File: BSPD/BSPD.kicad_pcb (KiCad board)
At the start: 2 copper layers, 81 x 61 mm, 34 parts, among them Q101 Q_PMOS_GSD, U101 641964-1, U102 641964-1, U103 R-78E5.0-0.5, U104 SN74LVC1G08DBVR, U105 LM339DR, U106 NE555DR, U107 SN74LVC3G14DCUR, U108 SN74AC32DR, U109 SN74LVC1G08DBVR, U110 641964-1, U111 641964-1

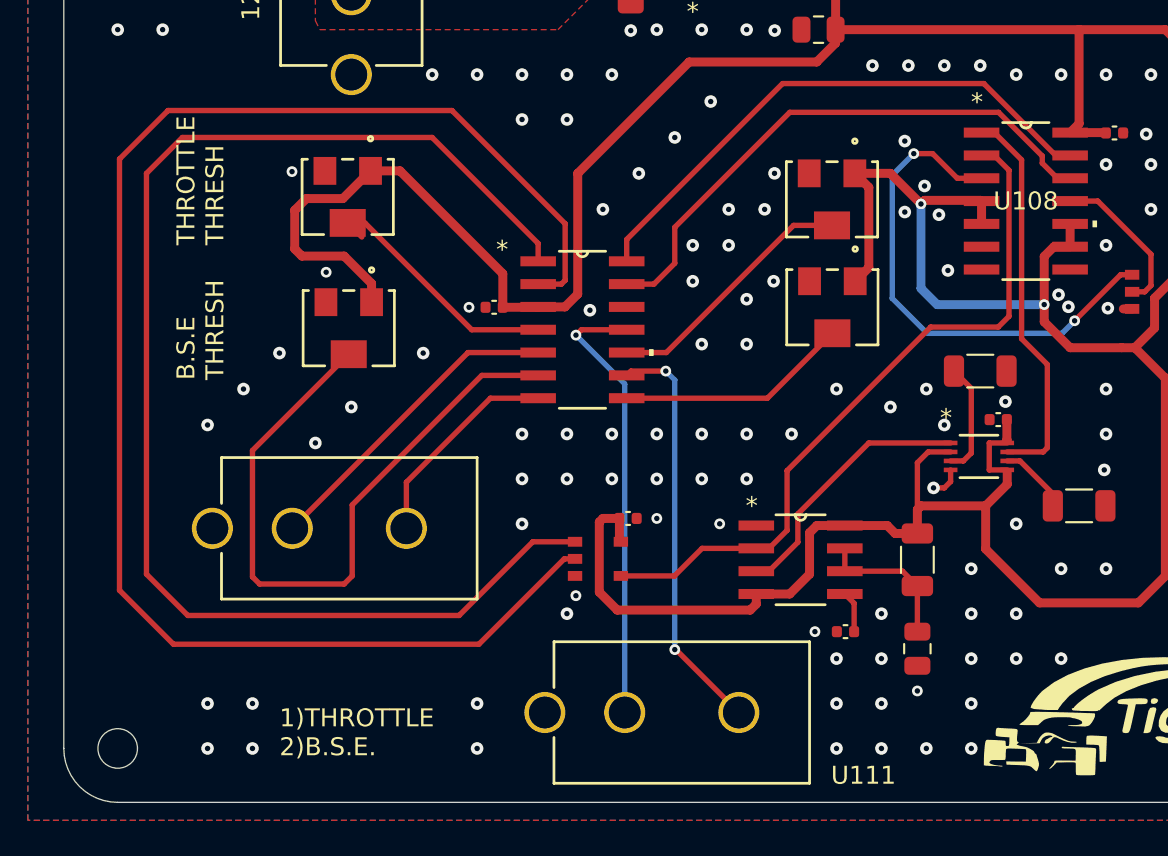
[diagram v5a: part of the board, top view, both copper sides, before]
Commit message: Fault Latch Updated and generated gerber files
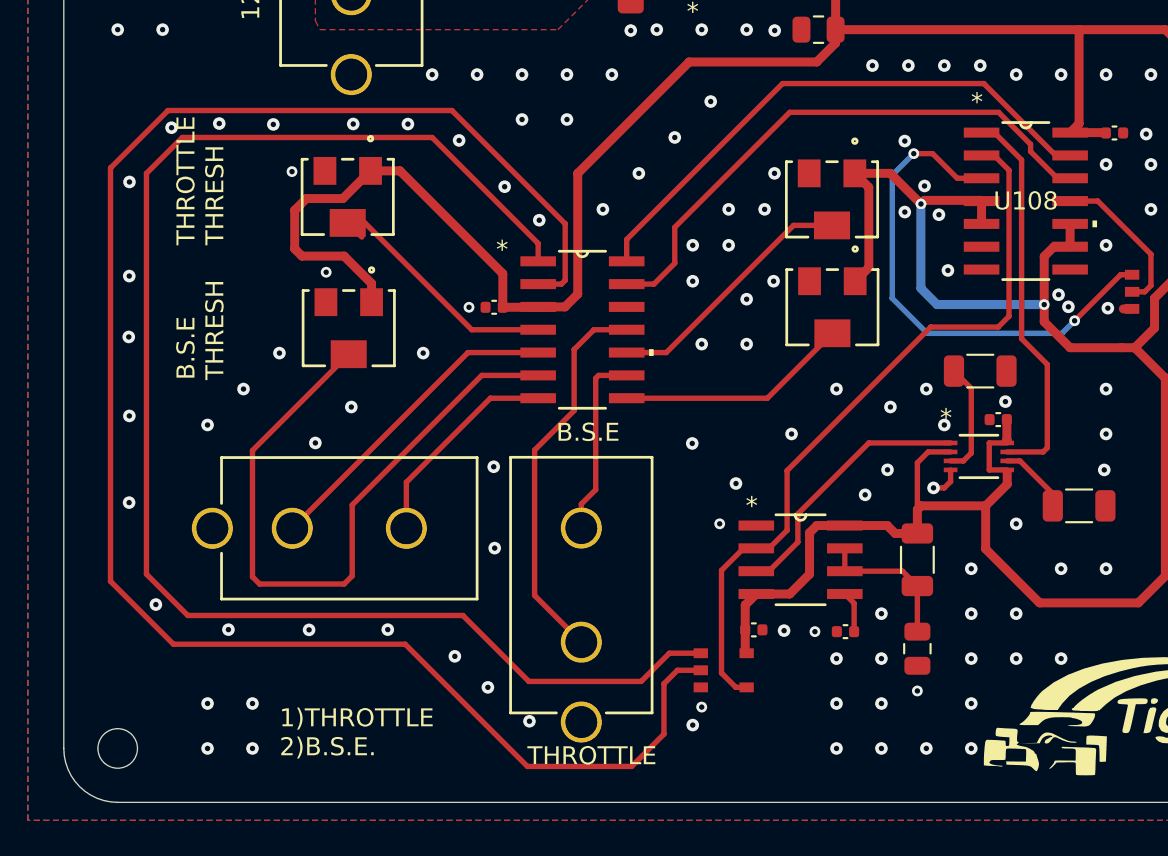
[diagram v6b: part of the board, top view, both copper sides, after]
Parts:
- U108: footprint LM339DR:D14 -> SN74AC32DR:D14
- moved C103 9.35 mm to (159.1, 126.5)
- moved U104 9.35 mm to (157.4, 128.8)
- moved U111 4.60 mm to (149.5, 127.2), turned to 90 degrees
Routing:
- net +5V: track 230.1 -> 217.4 mm
- net 2OUT: track 85.9 -> 98.0 mm
- net BSE_Sense_IN: track 23.0 -> 11.0 mm, vias 2 -> 0
- net 1OUT: track 74.9 -> 82.3 mm
- net THROTTLE_Sense_IN: track 25.1 -> 21.7 mm, vias 1 -> 0
- net Net-(U104-Y): track 39.5 -> 41.2 mm
- net GND: vias 268 -> 278
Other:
- board text added: "B.S.E"
- board text added: "THROTTLE"

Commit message: Labeling for clarithy
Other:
- board text added: "1)THRTL MIN VOLTAGE 2)B.S.E. MIN VOLTAGE"
- board text added: "1)THRTL SENSE 2)B.S.E. SENSE"
- board text added: "10% THROTTLE"
- board text added: "HARD BREAK"
- board text removed: "1)THROTTLE 2)B.S.E."
- board text removed: "B.S.E"
- board text removed: "THROTTLE"
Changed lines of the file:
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@@
 		(layer "Edge.Cuts")
 	)
-	(gr_text "1)THROTTLE\n2)B.S.E."
-		(at 132.7 133.6 0)
+	(gr_text "1)THRTL SENSE\n2)B.S.E. SENSE\n"
+		(at 151.2 134.6 0)
 		(layer "F.SilkS" knockout)
 		(effects
@@
 		)
 	)
-	(gr_text "B.S.E"
-		(at 148.1 116.1 0)
+	(gr_text "HARD \nBREAK\n"
+		(at 159.7 113.1 90)
 		(layer "F.SilkS" knockout)
 		(effects
 			(font
 				(size 1 1)
-				(thickness 0.125)
+				(thickness 0.1)
+			)
+			(justify left bottom)
+		)
+	)
+	(gr_text "1)THRTL MIN VOLTAGE\n2)B.S.E. MIN VOLTAGE\n"
+		(at 126.7 129.6 0)
+		(layer "F.SilkS" knockout)
+		(effects
+			(font
+				(size 1 1)
+				(thickness 0.1)
 			)
 			(justify left bottom)
@@
 				(size 1 1)
 				(thickness 0.1)
-			)
-			(justify left bottom)
-		)
-	)
-	(gr_text "THROTTLE"
-		(at 146.5 134.1 0)
-		(layer "F.SilkS" knockout)
-		(effects
-			(font
-				(size 1 1)
-				(thickness 0.125)
 			)
 			(justify left bottom)
@@
 		(layer "F.SilkS" knockout)
 		(effects
+			(font
+				(size 1 1)
+				(thickness 0.1)
+			)
+			(justify left bottom)
+		)
+	)
+	(gr_text "10%\nTHROTTLE\n"
+		(at 159.7 104.6 90)
+		(layer "F.SilkS" knockout)
+		(effects

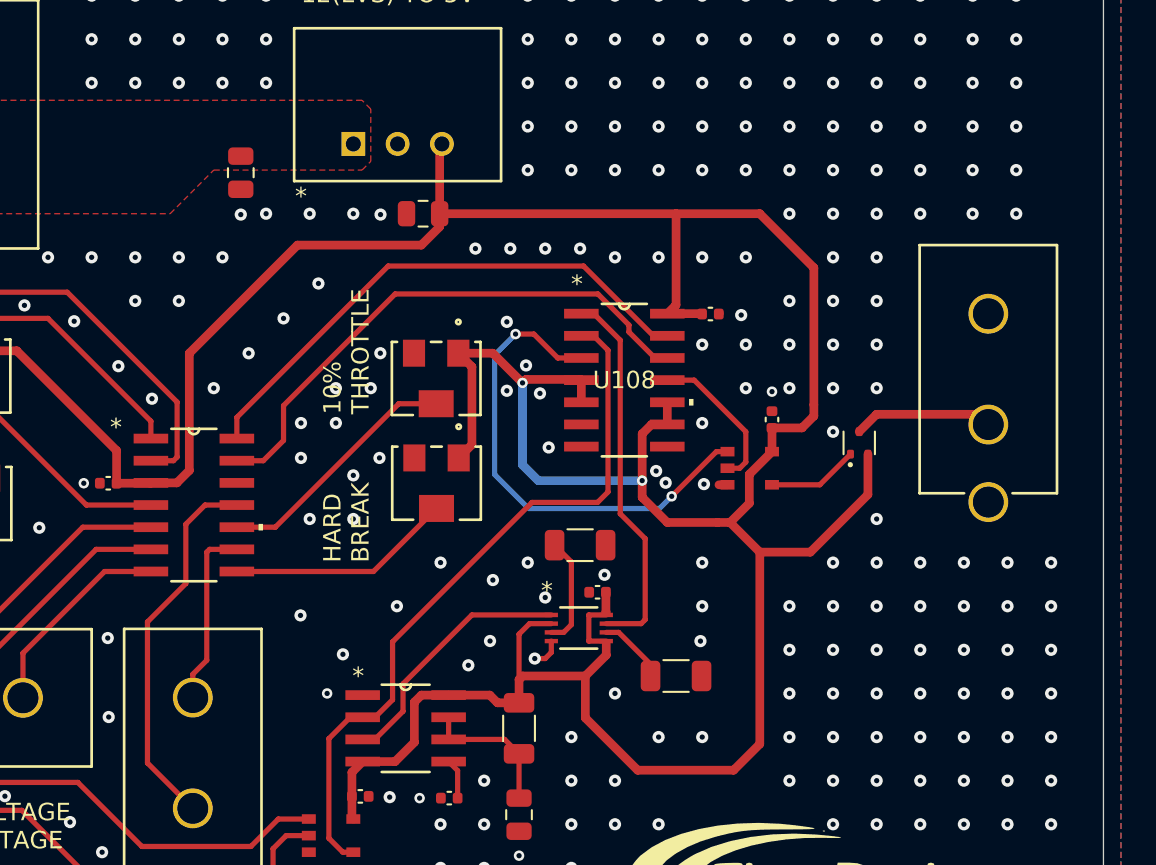
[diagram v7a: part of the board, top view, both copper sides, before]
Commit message: BSPD now active low output, fault latch rerouted.
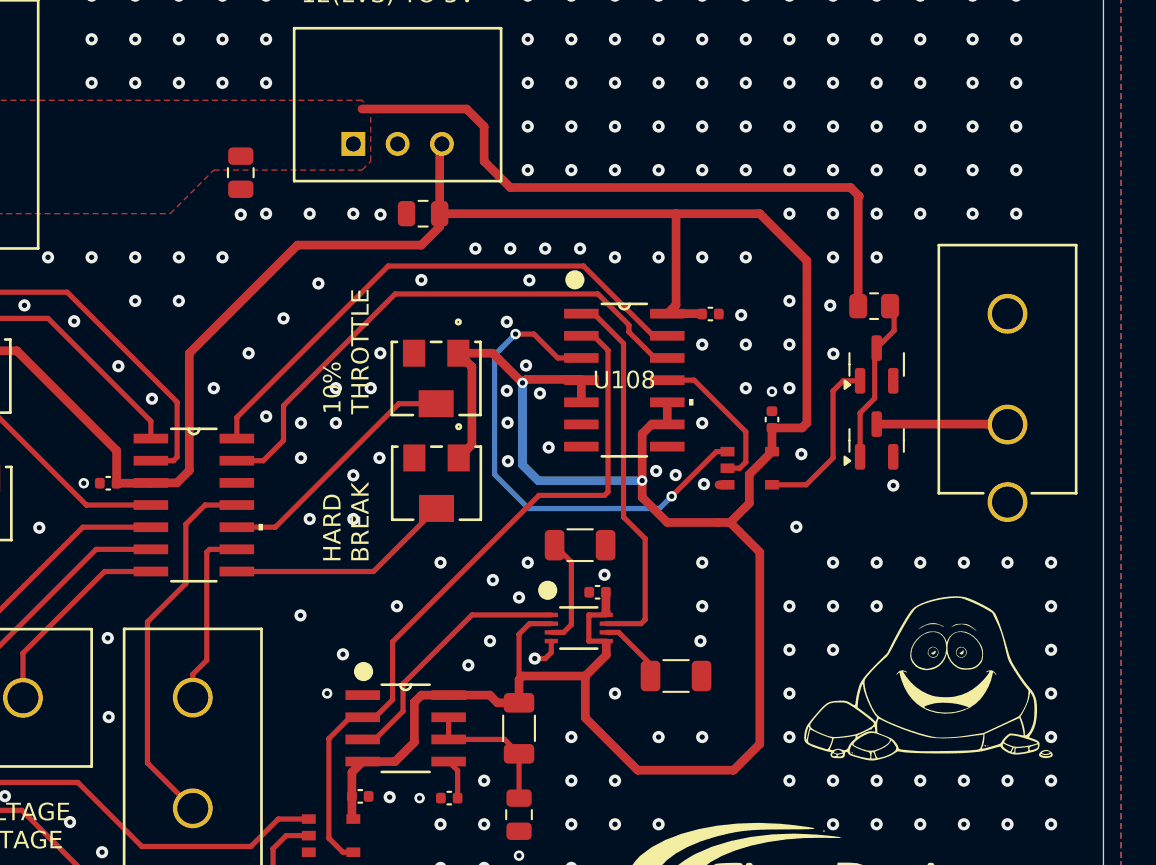
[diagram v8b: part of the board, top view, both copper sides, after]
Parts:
- removed Q101: Q_PMOS_GSD, Package_TO_SOT_SMD:SOT-523
- added G***: LOGO, LOGO, F.Cu at (191.7, 120.1)
- added Q1: Q_NMOS_GSD, Package_TO_SOT_SMD:SOT-23, F.Cu at (188.7, 101.7)
- added Q2: Q_NMOS_GSD, Package_TO_SOT_SMD:SOT-23, F.Cu at (188.7, 106.1)
- added R1: 10k, Resistor_SMD:R_0805_2012Metric, F.Cu at (188.6, 98.4)
- U108: footprint SN74AC32DR:D14 -> LM339DR:D14
- moved U110 1.10 mm to (196.2, 105.2)
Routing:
- net +12V: track 0.00 -> 38.1 mm
- net +5V: track 217.4 -> 207.1 mm
- net Net-(Q1-D): track 0.00 -> 9.70 mm
- net Net-(Q1-G): track 5.23 -> 9.77 mm
- net BSPD_TO_FAULT: track 8.05 -> 7.54 mm
- net GND: vias 278 -> 263
